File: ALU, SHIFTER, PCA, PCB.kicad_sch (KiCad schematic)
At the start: 14 parts

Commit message: updating to newest versions of schematics
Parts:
- removed unit 5 of E11
- removed E44: 74LS182, symbol 74xx:74LS182
- removed unit 3 of E58
- removed E68, E78: 74S153, DIP16, symbol Untitled-altium-import:root_0_74S153
- removed unit 5 of E76
- removed unit 1 of E76
- renumbered E42 to E60, E67 to E69, E66 to E70
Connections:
- net DAPF ALU04 H: no longer E60.9 (F0)
- net DAPF ALU05 H: no longer E60.10 (F1)
- net DAPD AMX01 H renamed DAPB AMX01 H
- net DAPD AMX02 H renamed DAPB AMX02 H
- net DAPD AMX03 H renamed DAPB AMX03 H
- net DAPF ALU06 H: no longer names the net of E60.11 (F2)
- net DAPF ALU07 H: no longer names the net of E60.13 (F3)

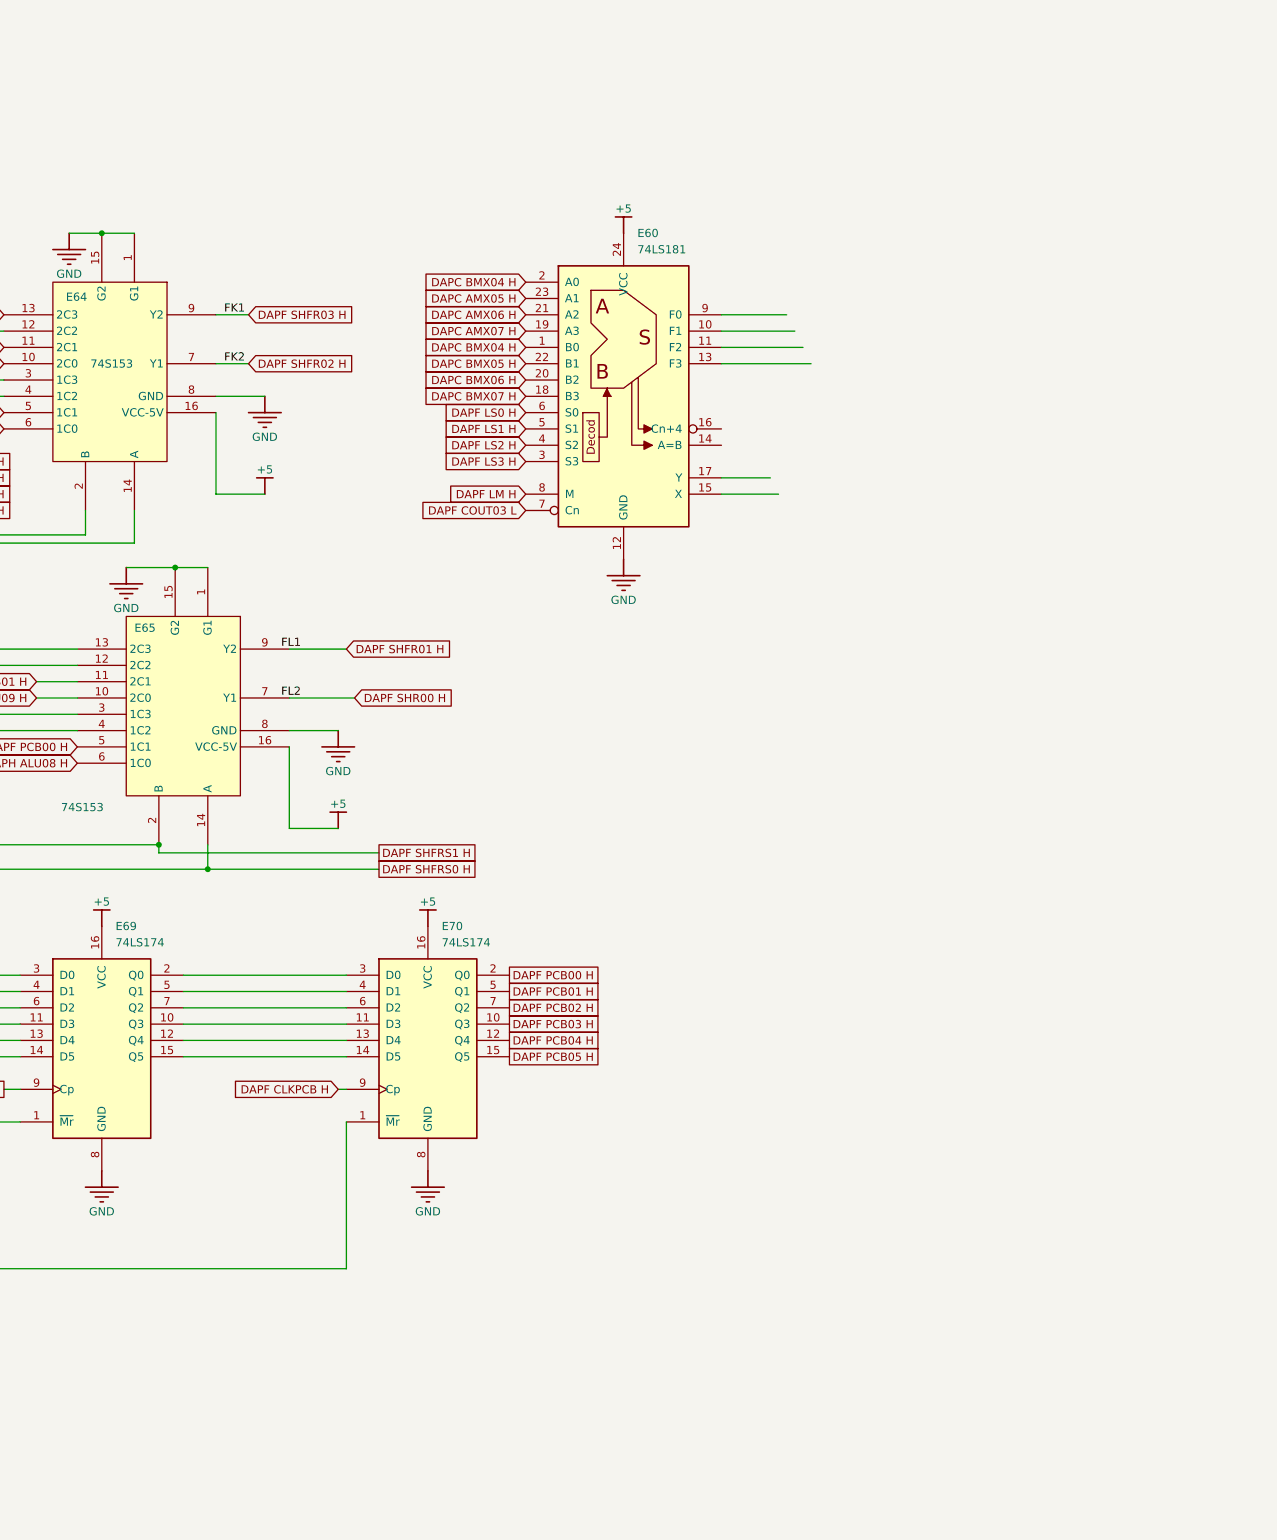
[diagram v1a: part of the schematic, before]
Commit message: Fixed net labels and added caps to BOM
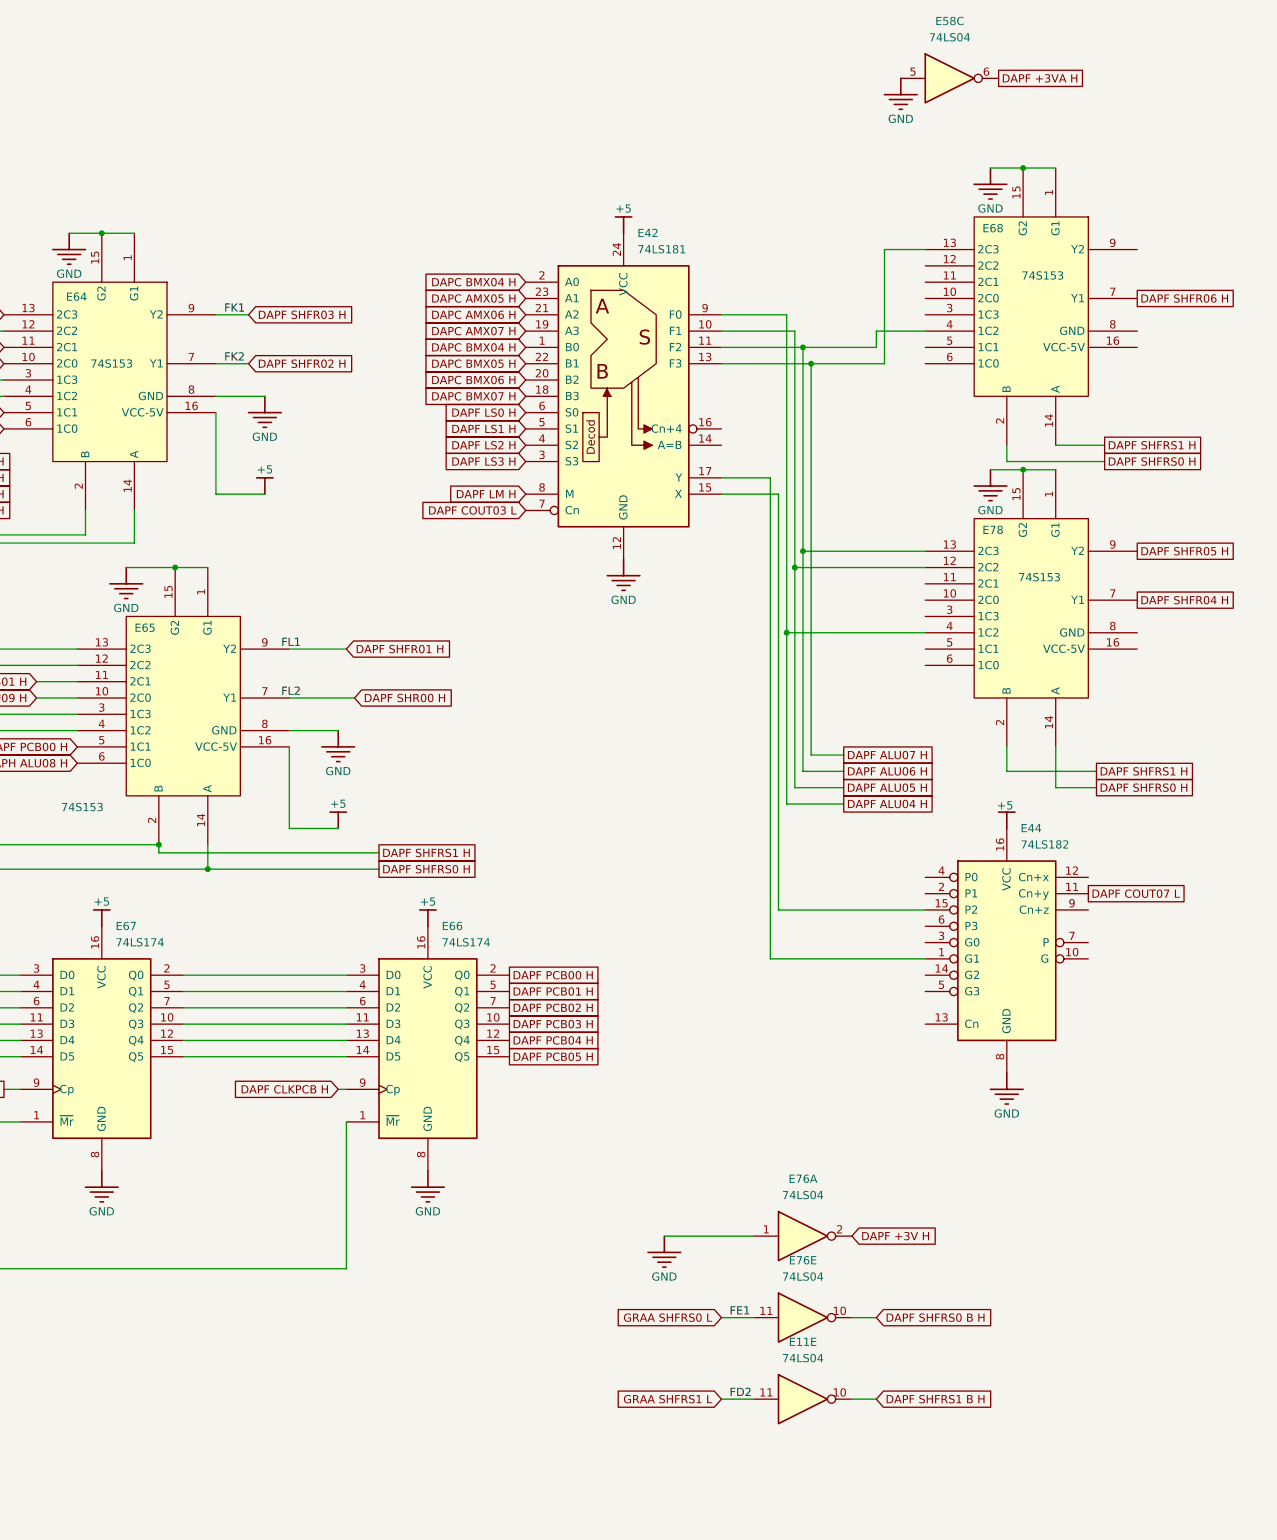
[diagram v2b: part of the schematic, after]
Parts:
- added unit 5 of E11
- added E44: 74LS182, symbol 74xx:74LS182
- added unit 3 of E58
- added E68, E78: 74S153, DIP16, symbol Untitled-altium-import:root_0_74S153
- added unit 5 of E76
- added unit 1 of E76
- renumbered E60 to E42, E70 to E66, E69 to E67
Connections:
- net +5: now also E44.16 (VCC)
- net DAPF +3V H: now also E76.2
- net DAPF ALU04 H: now also E42.9 (F0), E78.4 (1C2)
- net DAPF ALU05 H: now also E42.10 (F1), E78.12 (2C2)
- net DAPF SHFRS0 H: now also E68.2 (B), E78.14 (A)
- net DAPF SHFRS1 H: now also E68.14 (A), E78.2 (B)
- net GND: now also E44.8 (GND), E58.5, E68.1 (G1), E68.15 (G2), E76.1, E78.1 (G1), E78.15 (G2)
- net GRAA ALUS2 L: now also E76.11
- net GRAA ALUS3 L: now also E11.11
- net DAPF ALU06 H: now reaches E42.11 (F2)
- net DAPF ALU06 H: now also E68.4 (1C2), E78.13 (2C3)
- net DAPF ALU07 H: now reaches E42.13 (F3)
- net DAPF ALU07 H: now also E68.13 (2C3)
- net at E42.15 (X): now also E44.15 (P2)
- net at E42.17 (Y): now also E44.1 (G1)
- new net DAPF +3VA H: E58.6
- new net DAPF COUT07 L: E44.11 (Cn+y)
- new net DAPF SHFR04 H: E78.7 (Y1)
- new net DAPF SHFR05 H: E78.9 (Y2)
- new net DAPF SHFR06 H: E68.7 (Y1)
- new net DAPF SHFRS0  B H: E76.10
- new net DAPF SHFRS1 B H: E11.10
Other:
- title: (none) -> DATA PATHS
